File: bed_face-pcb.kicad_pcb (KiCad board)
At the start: 2 copper layers, 228.6 x 76.2 mm, 106 parts, among them SW1 SW_Push, U1 ProMicro

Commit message: added encoder spots, mounting holes, moved pro micro * standard mount holes interfered with pro micro * rewired after moving, changed some pins * fixed space footprint * began moving used footprints to bed-face-footprints
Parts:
- added BATTERY: BATTERY, Connector_JST:JST_PH_S2B-PH-K_1x02_P2.00mm_Horizontal, B.Cu at (93.2, 103.0)
- added H1: Hole, bed-face-components:standoff_hole, F.Cu at (54.0, 84.9)
- added H2: Hole, bed-face-components:standoff_hole, F.Cu at (54.0, 123.0)
- added H3: Hole, bed-face-components:standoff_hole, F.Cu at (149.2, 104.0)
- added H4: Hole, bed-face-components:standoff_hole, F.Cu at (244.5, 84.9)
- added H5: Hole, bed-face-components:standoff_hole, F.Cu at (244.5, 123.0)
- MX1, MX10, MX11, MX12, MX13, MX14, MX15, MX16, MX17, MX18, MX19, MX2, MX20, MX21, MX22, MX23, MX24, MX26, MX27, MX28, MX29, MX3, MX30, MX31, MX32, MX33, MX34, MX35, MX36, MX37, MX38, MX39, MX4, MX40, MX41, MX44, MX45, MX46, MX47, MX48, MX5, MX6, MX7, MX8, MX9: footprint MX_Only:MXOnly-1U-NoLED-EDIT -> bed-face-components:MXOnly-1U-NoLED-EDIT
- MX25: footprint MX_Only:MXOnly-1U-EDIT -> bed-face-components:MXOnly-1U-EDIT
- MX42: value LSPACE -> SPACE; footprint MX_Only:MXOnly-2U-ReversedStabilizers-NoLED-ComboSpace-EDIT -> bed-face-components:MXOnly-2U-ReversedStabilizers-NoLED-ComboSpace-EDIT
- MX43: footprint MX_Only:MXOnly-1U-NoLED-EDIT -> bed-face-components:MXOnly-1U-NoLED-EDIT-No-Corners
- SW1: value SW_Push -> RESET; footprint Keebio-Parts:SW_Tactile_SPST_Angled_MJTP1117 -> Keebio-Parts:SW_SPST_TL3342
- moved SW1 35.4 mm to (243.7, 69.0)
- moved D15 19.3 mm to (71.4, 94.5)
- moved D3 19.3 mm to (71.4, 75.4)
- moved D14 19.0 mm to (55.6, 94.5)
- moved D2 19.0 mm to (55.6, 75.4)
- moved U1 18.6 mm to (82.0, 81.8)
- moved D11 16.5 mm to (226.7, 75.4)
- moved D23 16.5 mm to (226.7, 94.5)
- moved D35 16.5 mm to (226.7, 113.5)
- moved D47 16.5 mm to (226.7, 132.6)
- moved D26 16.2 mm to (55.6, 113.5)
- moved D27 16.2 mm to (74.6, 113.5)
- moved D38 16.2 mm to (55.6, 132.6)
- moved D39 16.2 mm to (74.6, 132.6)
- moved MX42 9.53 mm to (149.2, 132.6)
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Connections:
- net +5V renamed VCC
- U1 pad 14: ROW3 -> COL3
- U1 pad 15: COL3 -> COL4
- U1 pad 24: BATT+ -> 4.7V
- U1 pad 9: COL4 -> ROW3
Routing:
- net 4.7V: track 0.00 -> 44.8 mm
- net COL8: track 289.6 -> 248.2 mm, vias 2 -> 0
- net COL4: track 247.2 -> 208.0 mm, vias 0 -> 1
- net ROW4: track 319.5 -> 297.6 mm, vias 2 -> 1
- net COL3: track 227.4 -> 206.4 mm
- net GND: track 36.3 -> 16.1 mm, vias 32 -> 31
- net COL6: track 263.4 -> 244.2 mm
- net COL0: track 80.2 -> 98.8 mm
- net COL9: track 224.2 -> 205.6 mm
- net COL7: track 223.1 -> 204.6 mm
- net COL5: track 263.8 -> 245.4 mm
- net LEDPIN: track 37.8 -> 55.8 mm, vias 0 -> 1
- net VCC: track 70.9 -> 82.1 mm
- net COL1: track 63.0 -> 72.9 mm
- net Net-(D3-Pad2): track 6.18 -> 14.5 mm
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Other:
- board text added: "-"

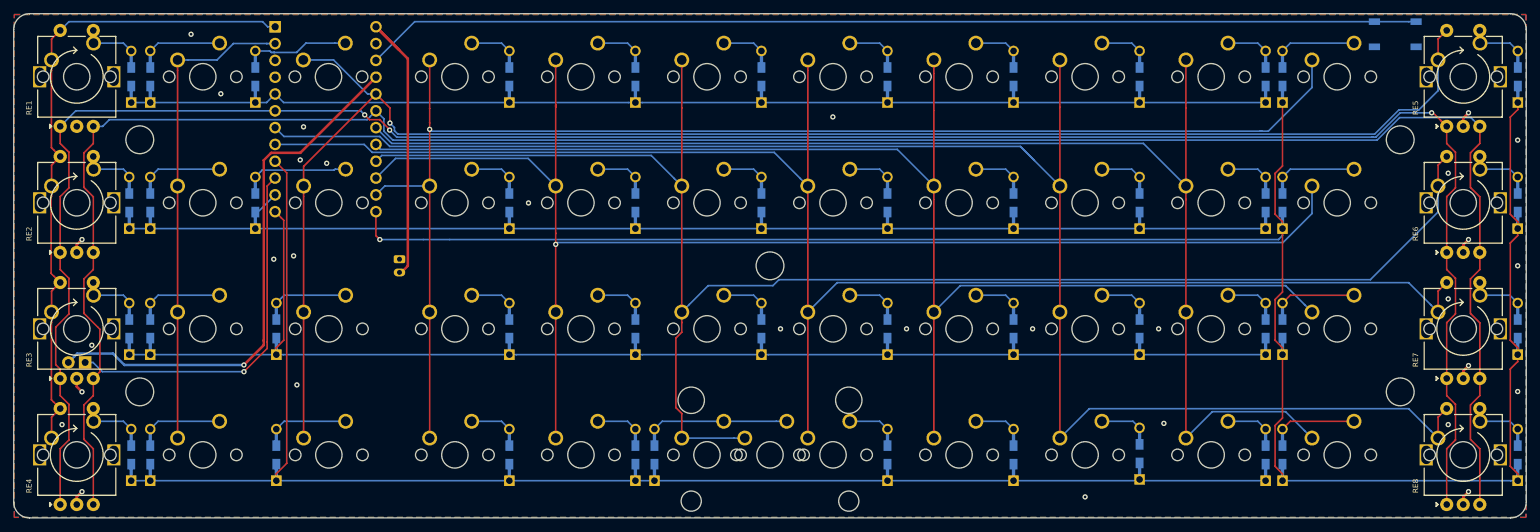
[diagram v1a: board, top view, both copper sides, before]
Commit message: added pads to f.mask, changed footprint silks, make SW1 th
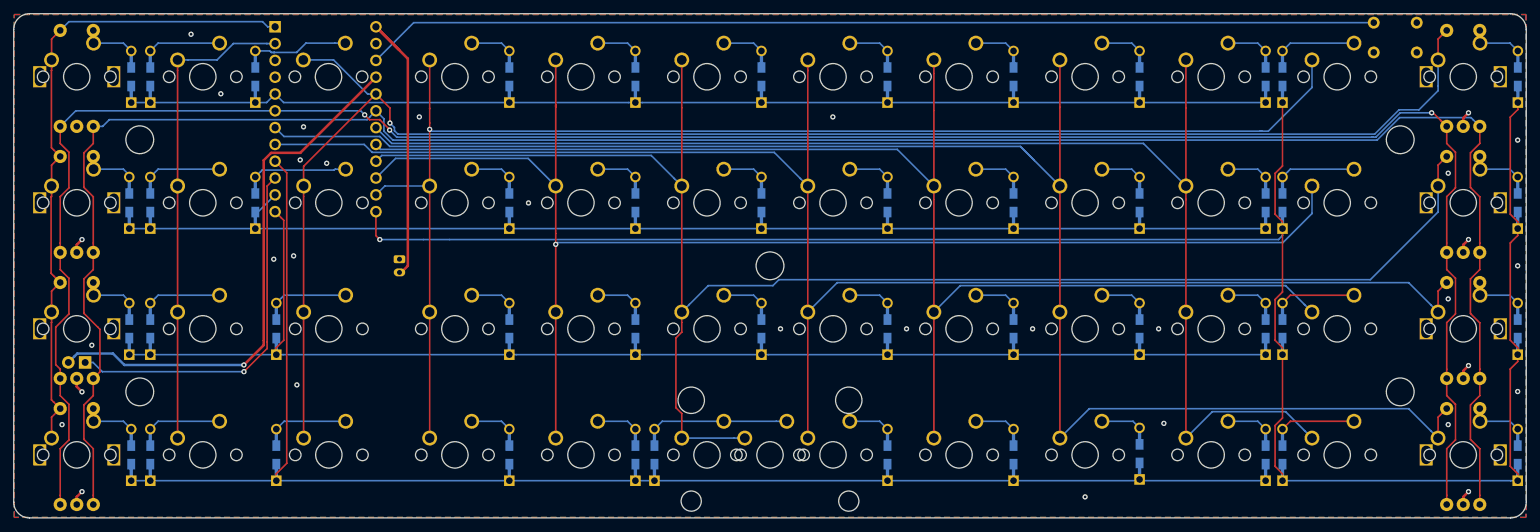
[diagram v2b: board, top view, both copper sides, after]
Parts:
- D1, D10, D11, D12, D13, D14, D15, D16, D17, D18, D19, D2, D20, D21, D22, D23, D24, D25, D26, D27, D28, D29, D3, D30, D31, D32, D33, D34, D35, D36, D37, D38, D39, D4, D40, D41, D42, D43, D44, D45, D46, D47, D48, D5, D6, D7, D8, D9: footprint Keebio-Parts:Diode-Hybrid-Back -> bed-face-components:Diode-Hybrid-Back-EDIT
- MX42: value SPACE -> LSPACE
- RE1, RE2, RE3, RE4, RE5, RE6, RE7, RE8: footprint reversible-kicad-footprints:MX-1U-EC11_Switch -> bed-face-components:EC11_Switch-EDIT
- SW1: footprint Keebio-Parts:SW_SPST_TL3342 -> random-keyboard-parts:PushButton_6x6mm_TH
- moved SW1 0.50 mm to (243.7, 69.5)
- renumbered BATTERY to J1
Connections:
- J1 pad 2: 4.7V -> Net-(J1-Pad2)
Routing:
- net RESET: track 159.6 -> 153.2 mm
- net GND: vias 31 -> 32

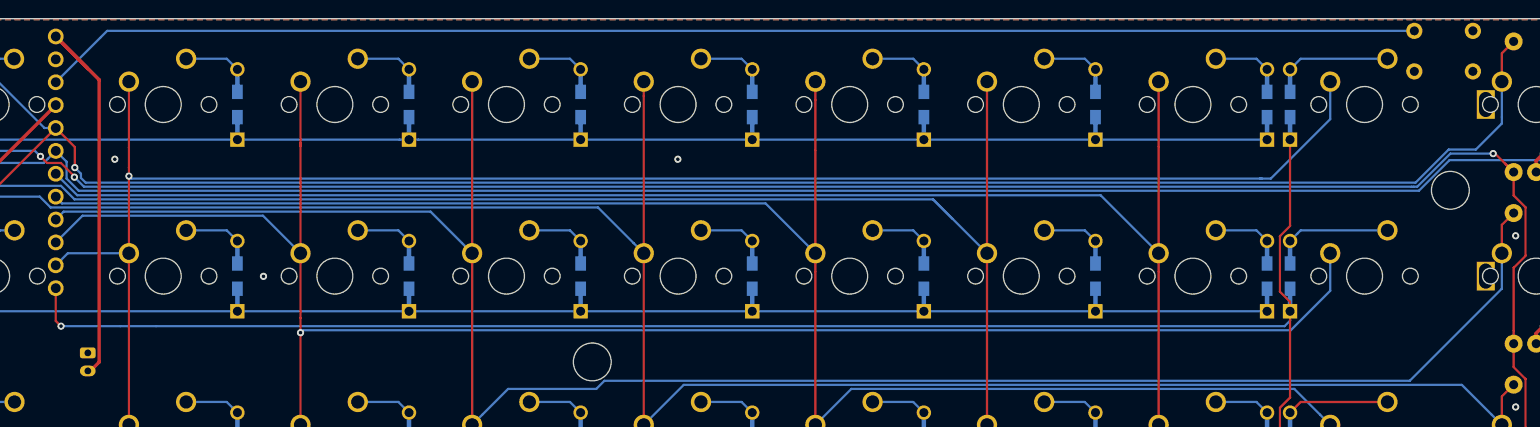
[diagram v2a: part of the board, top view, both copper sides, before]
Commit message: added miniature power switch * TODO closely check power pinout
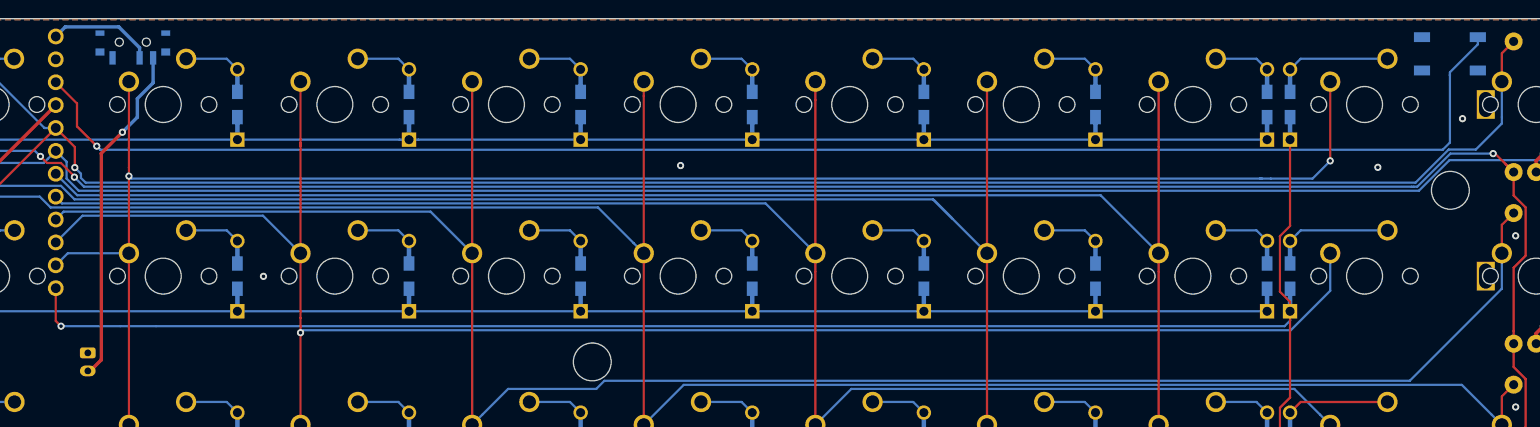
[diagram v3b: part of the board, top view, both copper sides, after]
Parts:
- added SW2: ON, bed-face-components:SWITCH_SPST_SMD_A-EDIT, B.Cu at (98.2, 68.5)
- SW1: footprint random-keyboard-parts:PushButton_6x6mm_TH -> random-keyboard-parts:SKQG-1155865
- moved SW1 0.76 mm to (244.4, 69.8), turned to 0 degrees
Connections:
- J1 pad 2: Net-(J1-Pad2) -> BATT+
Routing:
- net BATT+: track 0.00 -> 37.9 mm, vias 0 -> 1
- net 4.7V: track 44.8 -> 11.8 mm
- net RESET: track 153.2 -> 172.8 mm, vias 0 -> 1
- net COL3: track 206.4 -> 209.1 mm, vias 1 -> 2
- net GND: vias 32 -> 33

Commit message: finished tracking
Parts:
- MX41: footprint bed-face-components:MXOnly-1U-NoLED-EDIT -> bed-face-components:MXOnly-1U-2U-EDIT-LOWER
- MX44: footprint bed-face-components:MXOnly-1U-NoLED-EDIT -> bed-face-components:MXOnly-1U-2U-EDIT-RAISE
- moved D43 18.8 mm to (185.7, 132.6)
- moved D41 16.2 mm to (112.7, 132.6)
- moved D42 6.83 mm to (127.8, 138.1), turned to 180 degrees
- moved D44 2.88 mm to (188.9, 132.6)
- moved D45 0.19 mm to (205.1, 132.6)
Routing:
- net Net-(D43-Pad2): track 6.18 -> 30.8 mm
- net Net-(D41-Pad2): track 6.18 -> 20.5 mm
- net Net-(D44-Pad2): track 6.18 -> 18.6 mm
- net COL4: track 208.0 -> 218.3 mm
- net COL7: track 204.6 -> 214.1 mm
- net Net-(D42-Pad2): track 20.5 -> 28.0 mm
- net COL5: track 245.4 -> 247.5 mm
- net ROW3: track 221.3 -> 223.2 mm
- net COL6: track 244.2 -> 244.9 mm
- net GND: vias 33 -> 34
